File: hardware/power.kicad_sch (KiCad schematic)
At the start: 30 parts, among them J401 PRPC001DAAN-RC, J402 61300111121, J403 PRPC001DAAN-RC, J404 PRPC001DAAN-RC, J405 PRPC001DAAN-RC, U401 LM66200DRLR, U402 TPS63020DSJR

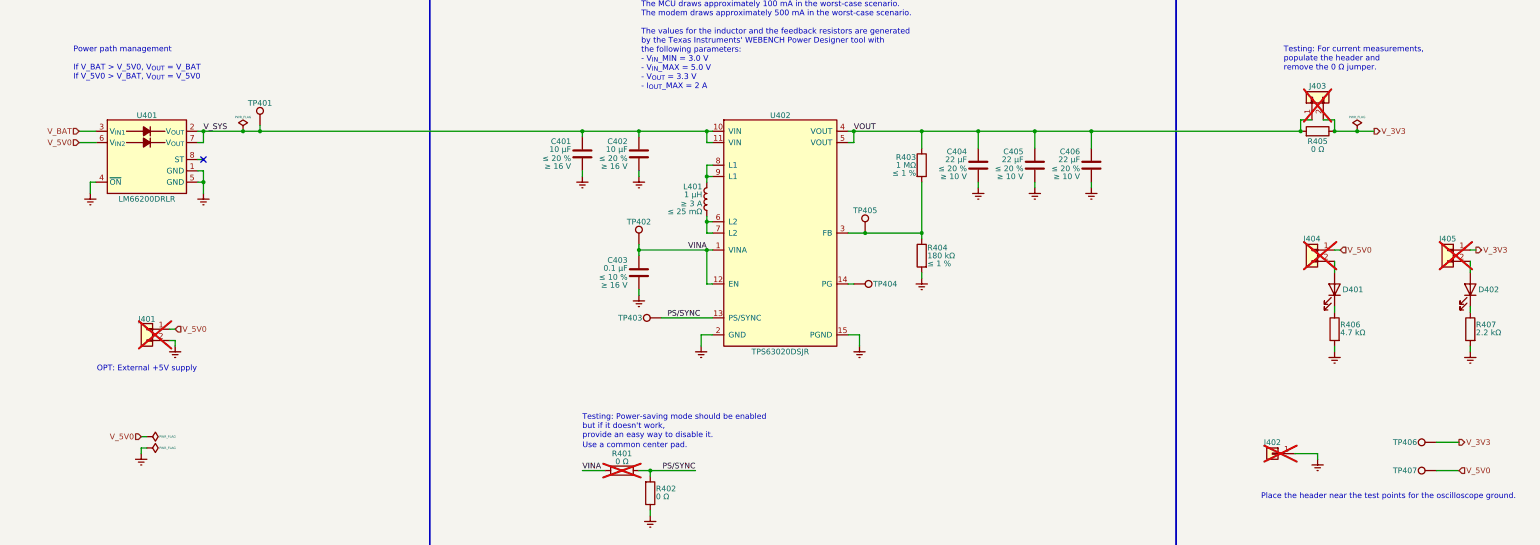
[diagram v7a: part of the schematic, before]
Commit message: HW: Refine power section
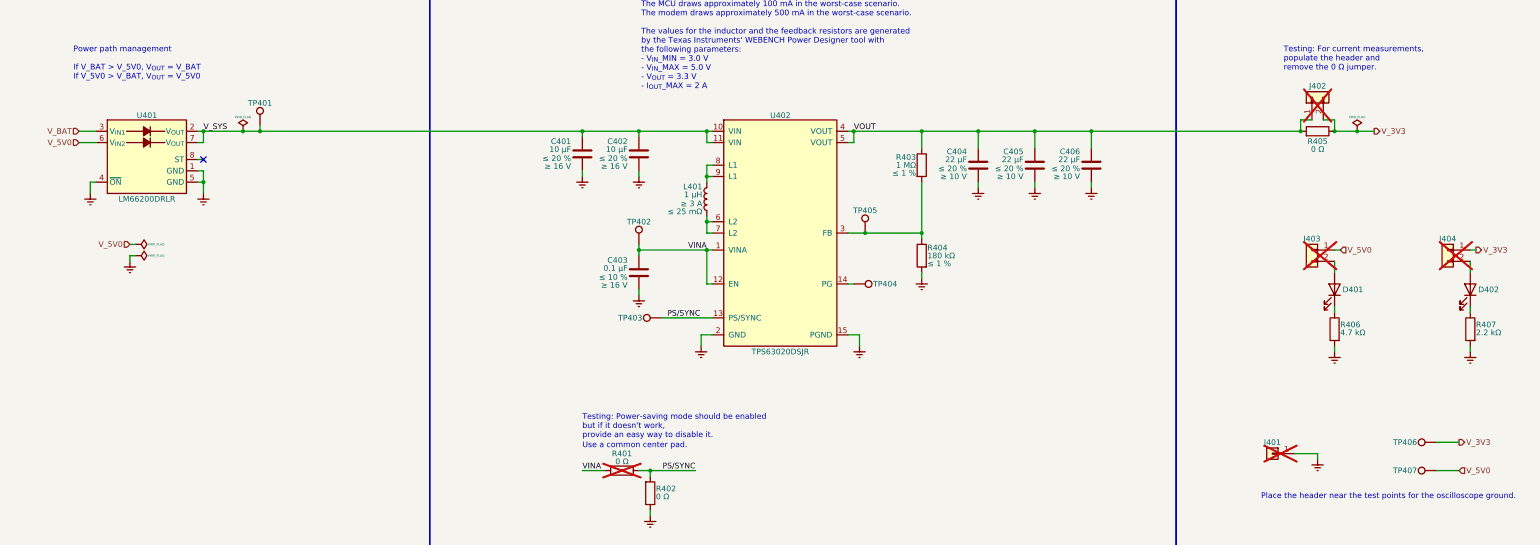
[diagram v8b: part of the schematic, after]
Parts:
- removed J401: PRPC001DAAN-RC, Connector_PinHeader_2.54mm:PinHeader_1x02_P2.54mm_Vertical, symbol Connector_Generic:Conn_01x02
- renumbered J402 to J401, J403 to J402, J404 to J403, J405 to J404
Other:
- note removed: "OPT: External +5V supply"
